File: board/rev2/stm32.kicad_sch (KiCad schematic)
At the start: 3 parts, among them U5 STM32U575VGTx, U7 TPD6S300A

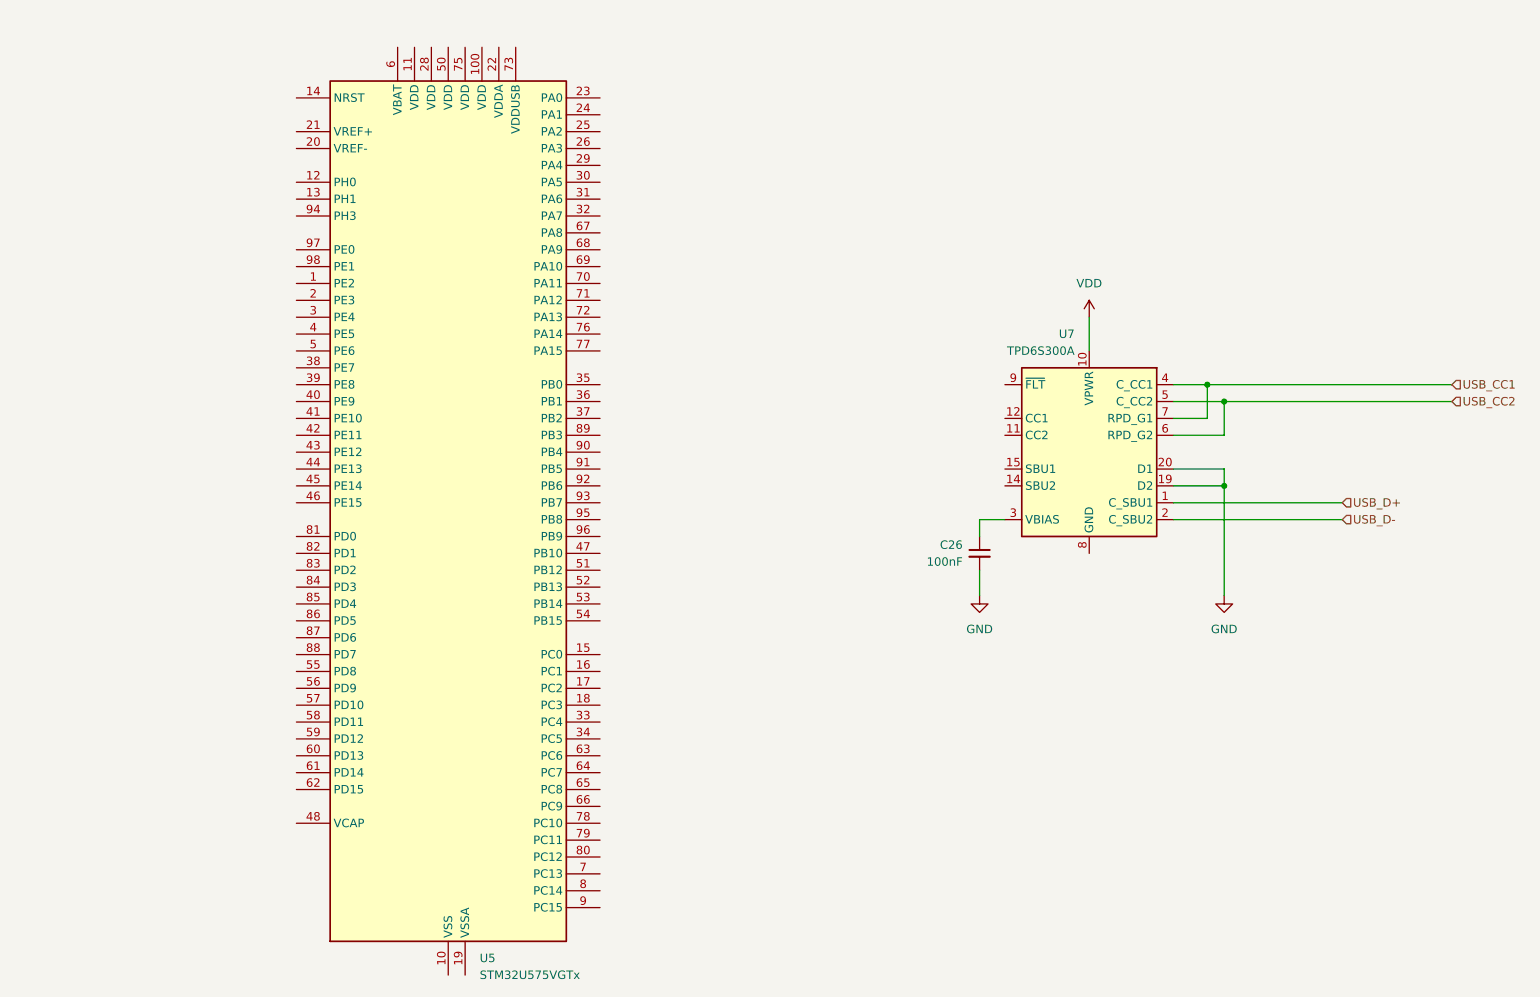
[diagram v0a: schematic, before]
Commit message: Continue board work
- move to rp2040, separate stm32g071 to do usb-c + aux ctrl IO
  - still cheaper lol with the cost of stm32s
- more power reg stuff
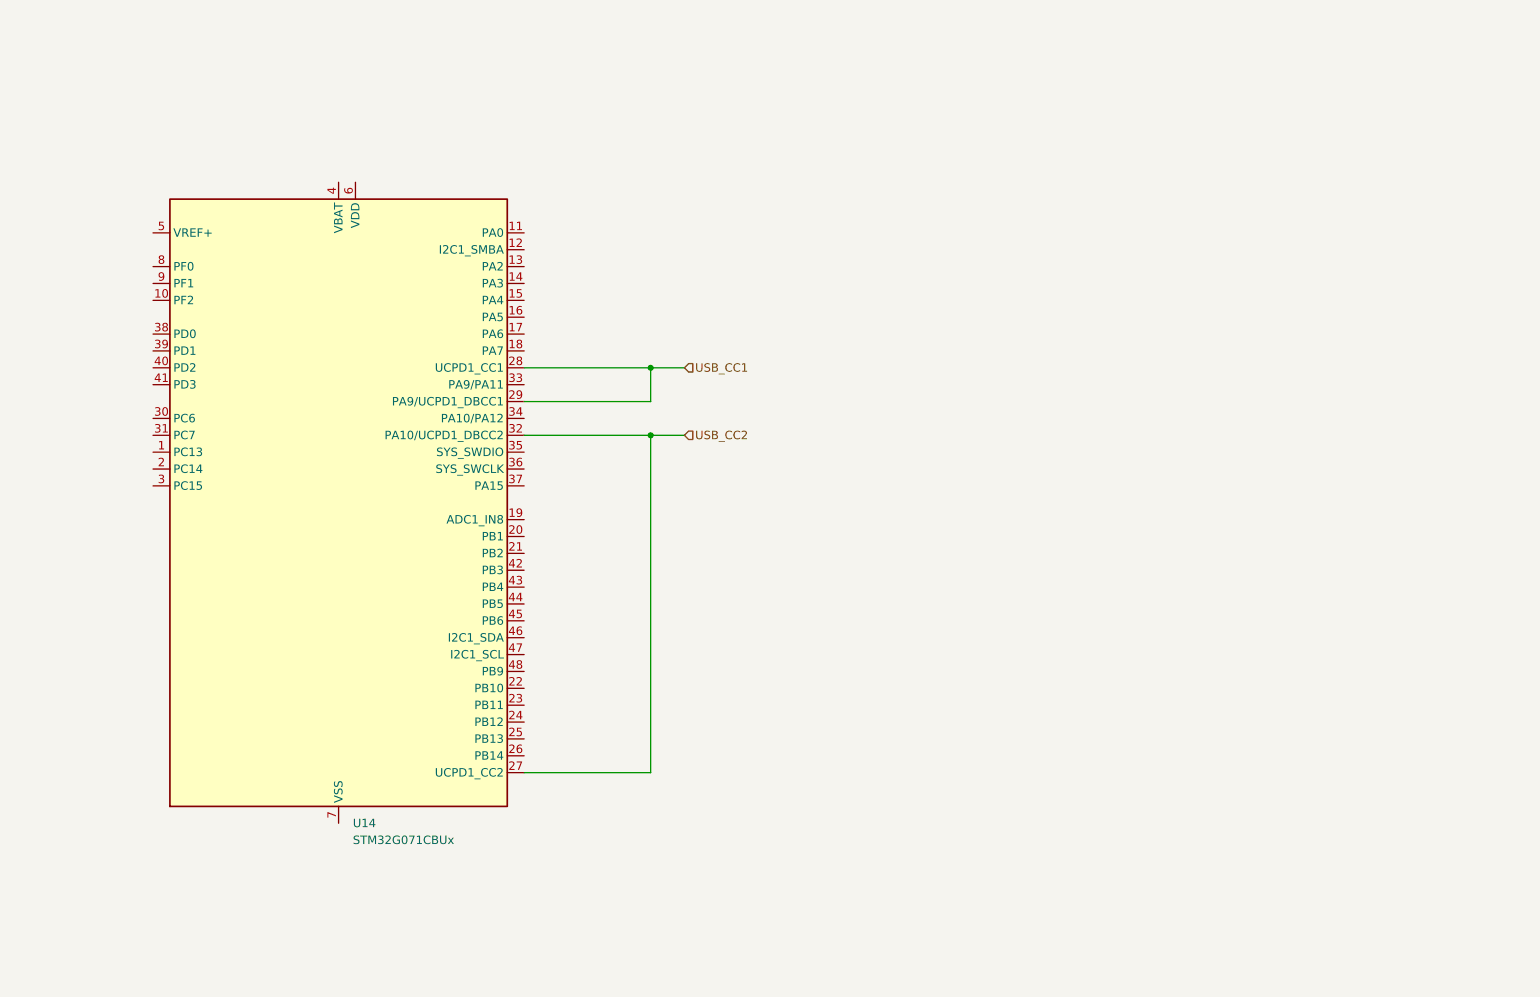
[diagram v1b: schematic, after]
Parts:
- removed C26: 100nF, symbol Device:C_Small
- removed U5: STM32U575VGTx, Package_QFP:LQFP-100_14x14mm_P0.5mm, symbol MCU_ST_STM32U5:STM32U575VGTx
- removed U7: TPD6S300A, Package_DFN_QFN:WQFN-20-1EP_3x3mm_P0.4mm_EP1.7x1.7mm_ThermalVias, symbol Power_Protection:TPD6S300A
- added U14: STM32G071CBUx, Package_DFN_QFN:QFN-48-1EP_7x7mm_P0.5mm_EP5.6x5.6mm, symbol MCU_ST_STM32G0:STM32G081CBUx
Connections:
- net USB_CC1: now also U14.28 (PA8), U14.29 (PA9/UCPD1_DBCC1)
- net USB_CC2: now also U14.27 (PB15), U14.32 (PA10/UCPD1_DBCC2)
- new net: U14.49 (VSS), U14.7 (VSS)

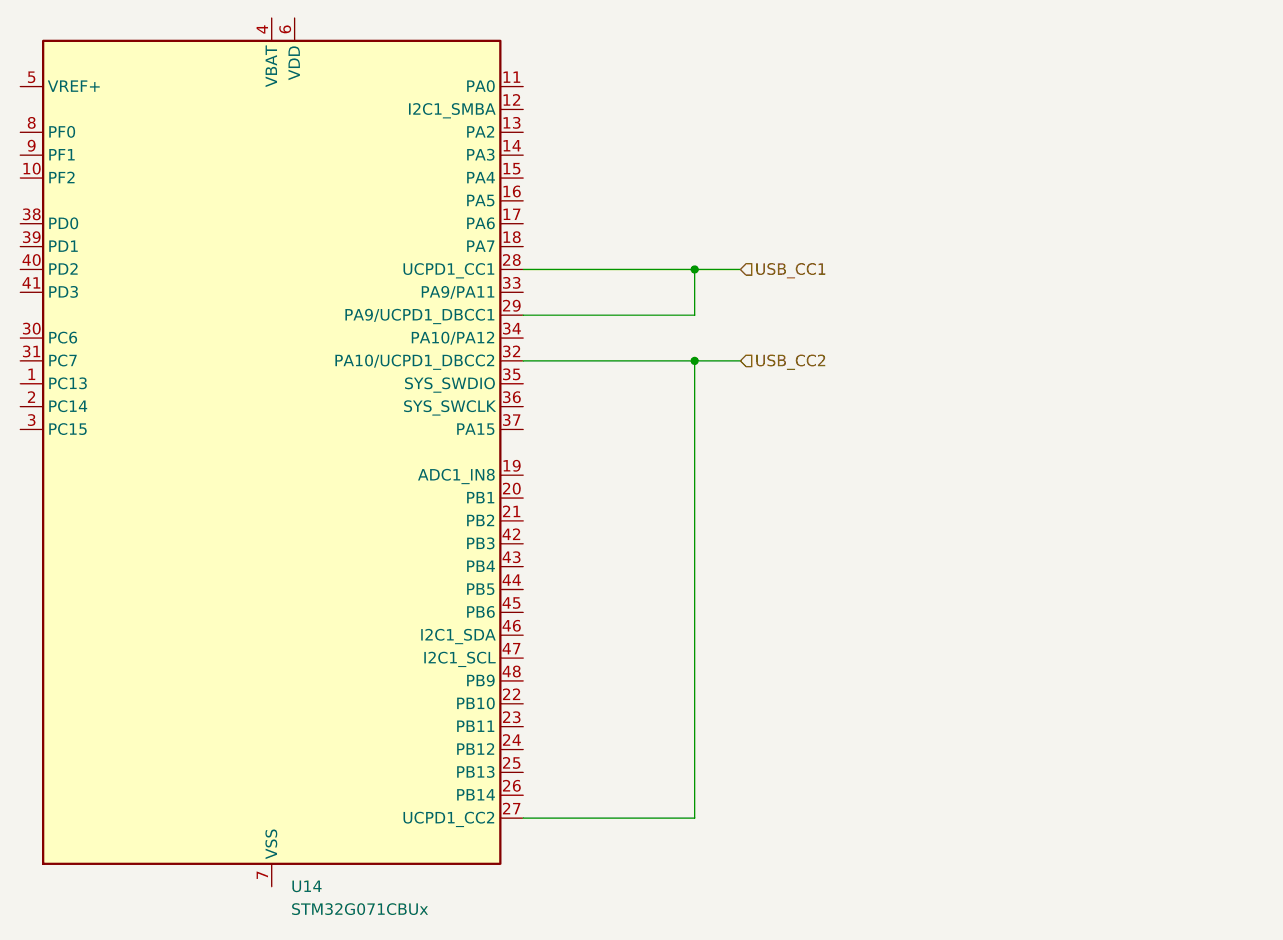
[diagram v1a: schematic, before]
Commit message: Split out board into A/B
allow 2x displays (for chaining)
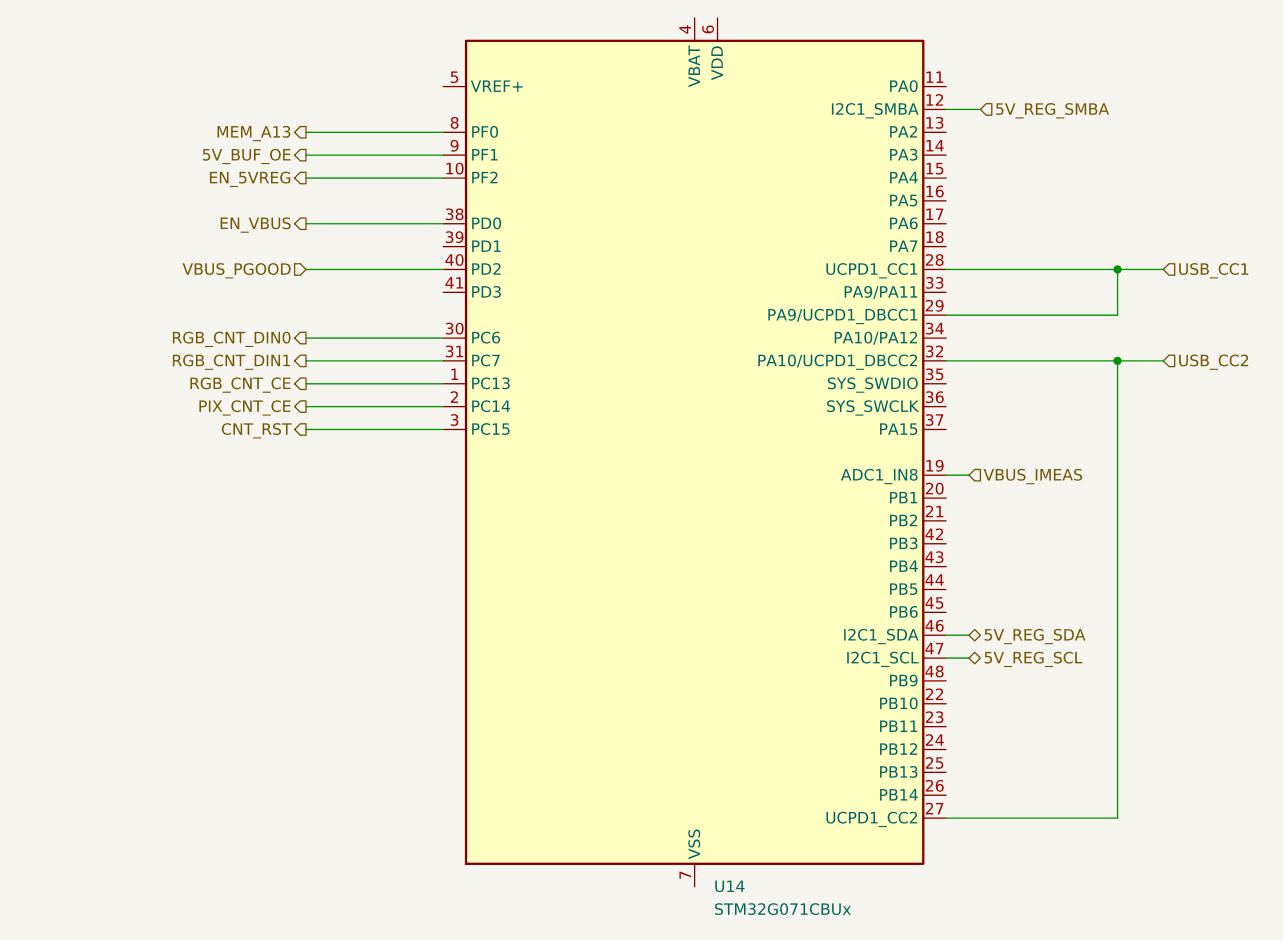
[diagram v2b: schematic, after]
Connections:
- net RGB_CNT_CE: now reaches U14.1 (PC13)
- net EN_5VREG: now reaches U14.10 (PF2)
- net 5V_REG_SMBA: now reaches U14.12 (PA1)
- net VBUS_IMEAS: now reaches U14.19 (PB0)
- net PIX_CNT_CE: now reaches U14.2 (PC14)
- net CNT_RST: now reaches U14.3 (PC15)
- net RGB_CNT_DIN0: now reaches U14.30 (PC6)
- net RGB_CNT_DIN1: now reaches U14.31 (PC7)
- net EN_VBUS: now reaches U14.38 (PD0)
- net VBUS_PGOOD: now reaches U14.40 (PD2)
- net 5V_REG_SDA: now reaches U14.46 (PB7)
- net 5V_REG_SCL: now reaches U14.47 (PB8)
- net MEM_A13: now reaches U14.8 (PF0)
- net 5V_BUF_OE: now reaches U14.9 (PF1)
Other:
- moved on the sheet: U14

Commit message: More board work
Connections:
- net COMM0.TX: now reaches U14.13 (PA2)
- net COMM0.RX: now reaches U14.14 (PA3)
- net PIX_CNT_PE: now reaches U14.24 (PB12)
- net COMM1.TX: now reaches U14.33 (PA9/PA11)
- net COMM1.RX: now reaches U14.34 (PA10/PA12)
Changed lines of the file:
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@@
 		(color 0 0 0 0)
 	)
+	(bus_entry
+		(at 209.55 82.55)
+		(size -2.54 2.54)
+		(stroke
+			(width 0)
+			(type default)
+		)
+	)
+	(bus_entry
+		(at 209.55 77.47)
+		(size -2.54 2.54)
+		(stroke
+			(width 0)
+			(type default)
+		)
+	)
+	(bus_entry
+		(at 209.55 59.69)
+		(size -2.54 2.54)
+		(stroke
+			(width 0)
+			(type default)
+		)
+	)
+	(bus_entry
+		(at 209.55 62.23)
+		(size -2.54 2.54)
+		(stroke
+			(width 0)
+			(type default)
+		)
+	)
+	(wire
+		(pts
+			(xy 158.75 62.23) (xy 207.01 62.23)
+		)
+		(stroke
+			(width 0)
+			(type default)
+		)
+	)
+	(bus
+		(pts
+			(xy 209.55 67.31) (xy 209.55 77.47)
+		)
+		(stroke
+			(width 0)
+			(type default)
+		)
+	)
 	(wire
 		(pts
@@
 		)
 	)
+	(bus
+		(pts
+			(xy 209.55 48.26) (xy 209.55 59.69)
+		)
+		(stroke
+			(width 0)
+			(type default)
+		)
+	)
 	(wire
 		(pts
@@
 	(wire
 		(pts
-			(xy 177.8 87.63) (xy 182.88 87.63)
+			(xy 177.8 87.63) (xy 180.34 87.63)
 		)
 		(stroke
@@
 	(wire
 		(pts
-			(xy 177.8 77.47) (xy 182.88 77.47)
+			(xy 177.8 77.47) (xy 180.34 77.47)
 		)
 		(stroke
@@
 		)
 	)
+	(bus
+		(pts
+			(xy 214.63 67.31) (xy 209.55 67.31)
+		)
+		(stroke
+			(width 0)
+			(type default)
+		)
+	)
 	(wire
 		(pts
@@
 	(wire
 		(pts
+			(xy 158.75 59.69) (xy 180.34 59.69)
+		)
+		(stroke
+			(width 0)
+			(type default)
+		)
+	)
+	(wire
+		(pts
 			(xy 87.63 85.09) (xy 102.87 85.09)
 		)
@@
 		)
 	)
+	(bus
+		(pts
+			(xy 215.9 48.26) (xy 209.55 48.26)
+		)
+		(stroke
+			(width 0)
+			(type default)
+		)
+	)
 	(wire
 		(pts
@@
 		)
 	)
-	(wire
-		(pts
-			(xy 162.56 59.69) (xy 158.75 59.69)
+	(bus
+		(pts
+			(xy 209.55 59.69) (xy 209.55 62.23)
 		)
 		(stroke
@@
 	(wire
 		(pts
+			(xy 158.75 64.77) (xy 207.01 64.77)
+		)
+		(stroke
+			(width 0)
+			(type default)
+		)
+	)
+	(wire
+		(pts
+			(xy 158.75 85.09) (xy 207.01 85.09)
+		)
+		(stroke
+			(width 0)
+			(type default)
+		)
+	)
+	(bus
+		(pts
+			(xy 209.55 77.47) (xy 209.55 82.55)
+		)
+		(stroke
+			(width 0)
+			(type default)
+		)
+	)
+	(wire
+		(pts
 			(xy 161.29 120.65) (xy 158.75 120.65)
 		)
@@
 	(wire
 		(pts
+			(xy 161.29 130.81) (xy 158.75 130.81)
+		)
+		(stroke
+			(width 0)
+			(type default)
+		)
+	)
+	(wire
+		(pts
+			(xy 158.75 80.01) (xy 207.01 80.01)
+		)
+		(stroke
+			(width 0)
+			(type default)
+		)
+	)
+	(wire
+		(pts
 			(xy 158.75 77.47) (xy 177.8 77.47)
 		)
@@
 			(width 0)
 			(type default)
+		)
+	)
+	(label "COMM1.TX"
+		(at 196.85 80.01 0)
+		(effects
+			(font
+				(size 1.27 1.27)
+			)
+			(justify left bottom)
+		)
+	)
+	(label "COMM1.RX"
+		(at 196.85 85.09 0)
+		(effects
+			(font
+				(size 1.27 1.27)
+			)
+			(justify left bottom)
+		)
+	)
+	(label "COMM0.RX"
+		(at 196.85 64.77 0)
+		(effects
+			(font
+				(size 1.27 1.27)
+			)
+			(justify left bottom)
+		)
+	)
+	(label "COMM0.TX"
+		(at 196.85 62.23 0)
+		(effects
+			(font
+				(size 1.27 1.27)
+			)
+			(justify left bottom)
 		)
 	)
@@
 		)
 	)
+	(hierarchical_label "PIX_CNT_PE"
+		(shape output)
+		(at 161.29 130.81 0)
+		(effects
+			(font
+				(size 1.27 1.27)
+			)
+			(justify left)
+		)
+	)
 	(hierarchical_label "RGB_CNT_DIN0"
 		(shape output)
@@
 		)
 	)
+	(hierarchical_label "COMM1{TX RX}"
+		(shape bidirectional)
+		(at 214.63 67.31 0)
+		(effects
+			(font
+				(size 1.27 1.27)
+			)
+			(justify left)
+		)
+	)
 	(hierarchical_label "USB_CC2"
 		(shape input)
-		(at 182.88 87.63 0)
+		(at 180.34 87.63 0)
 		(effects
 			(font
@@
 	(hierarchical_label "5V_REG_SMBA"
 		(shape input)
-		(at 162.56 59.69 0)
+		(at 180.34 59.69 0)
 		(effects
 			(font
@@
 			)
 			(justify right)
+		)
+	)
+	(hierarchical_label "COMM0{TX RX}"
+		(shape bidirectional)
+		(at 215.9 48.26 0)
+		(effects
+			(font
+				(size 1.27 1.27)
+			)
+			(justify left)
 		)
 	)
 	(hierarchical_label "USB_CC1"
 		(shape input)
-		(at 182.88 77.47 0)
+		(at 180.34 77.47 0)
 		(effects
 			(font
@@
 		)
 		(pin "33"
+			(alternate "USART1_TX (PA9)")
 		)
 		(pin "12"
@@
 		)
 		(pin "34"
+			(alternate "USART1_RX (PA10)")
 		)
 		(pin "45"
@@
 		)
 		(pin "13"
+			(alternate "USART2_TX")
 		)
 		(pin "7"
 		)
 		(pin "14"
+			(alternate "USART2_RX")
 		)
 		(pin "17"

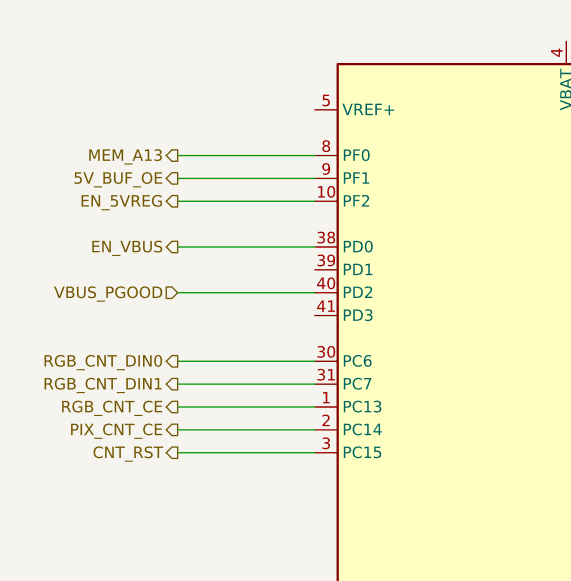
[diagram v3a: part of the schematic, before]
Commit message: Board GPIO allocation
- and usbmux

still need to do termination on the big buses + a bunch of bypass caps
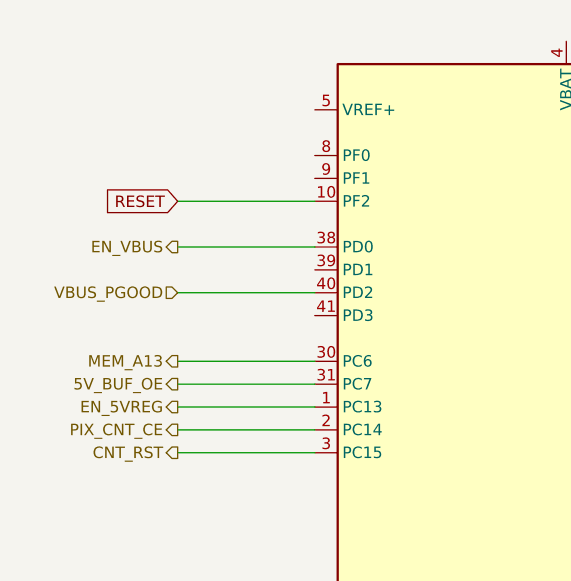
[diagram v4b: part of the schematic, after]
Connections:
- net RGB_CNT_CE is gone; now on net EN_5VREG: U14.1 (PC13)
- net RGB_CNT_DIN0 is gone; now on net MEM_A13: U14.30 (PC6)
- net RGB_CNT_DIN1 is gone; now on net 5V_BUF_OE: U14.31 (PC7)
- net 5V_BUF_OE: no longer U14.9 (PF1)
- net EN_5VREG: no longer U14.10 (PF2)
- net MEM_A13: no longer U14.8 (PF0)
- new net RESET: U14.10 (PF2)
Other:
- company: (none) -> MLABS
- title: (none) -> Power Supply (+aux Decoder IO) Microcontroller
